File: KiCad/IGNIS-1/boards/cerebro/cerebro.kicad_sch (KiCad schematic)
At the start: 22 parts, among them J1 LiPo_1S_in, J2 RBF_pin, J40 Backplane_2x10, Q1 MMBT3904, SW1 Main_SW, U1 Prot_1S_UVLO_OCP, U10 ESP32-WROOM DevKit 38p, U2 BuckBoost_3V3, U3 Boost_5V

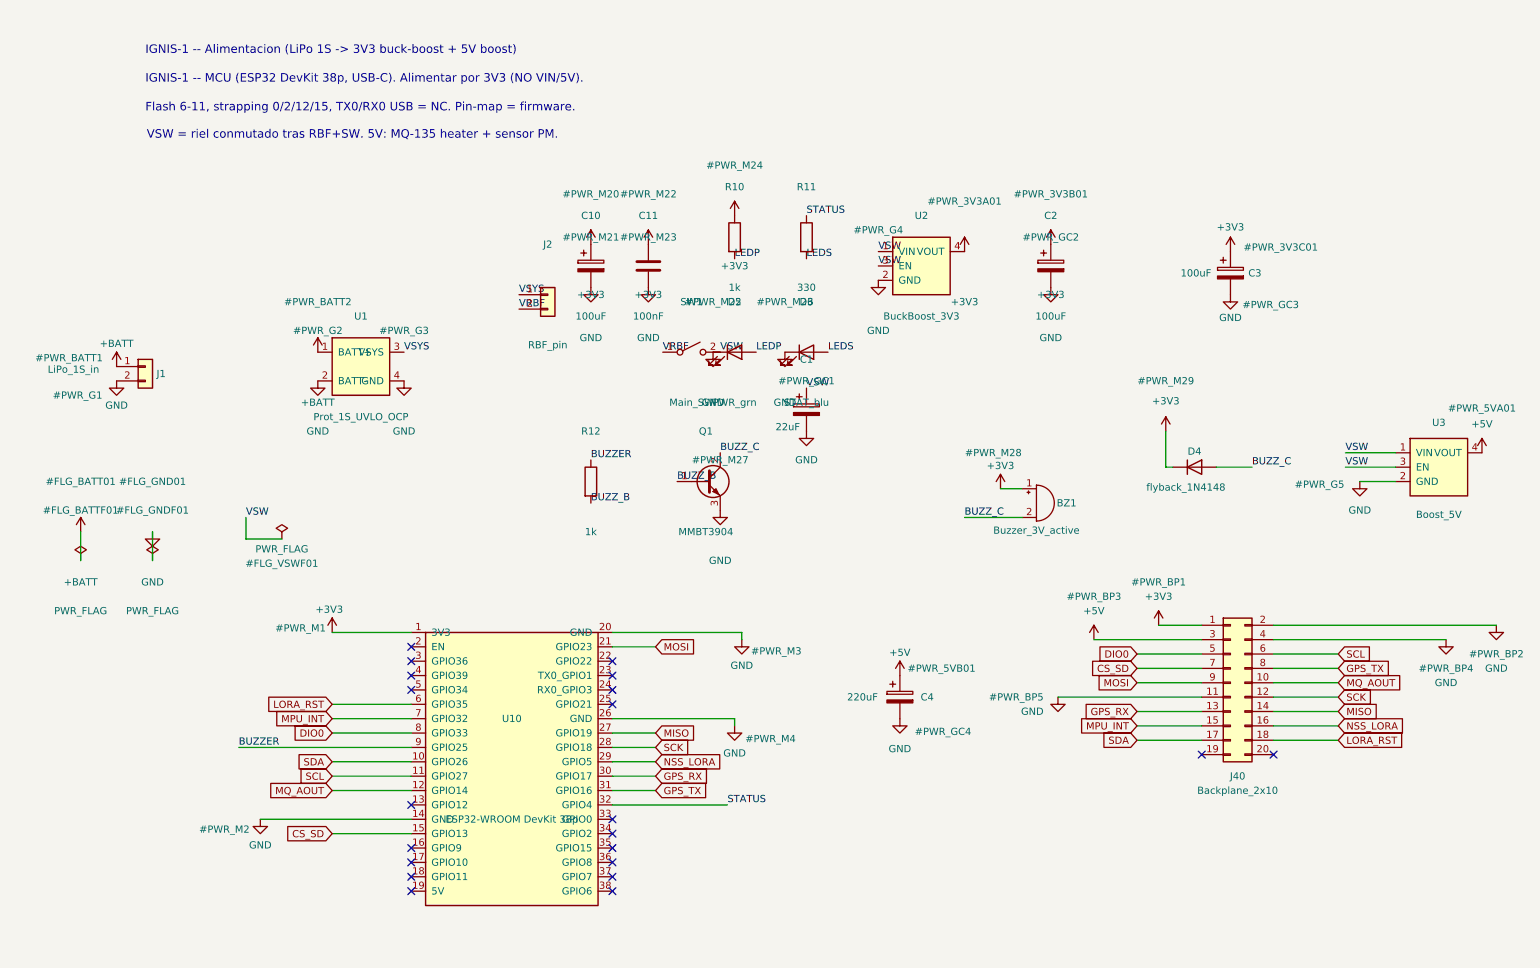
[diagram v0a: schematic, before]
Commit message: PCB del MCU creado
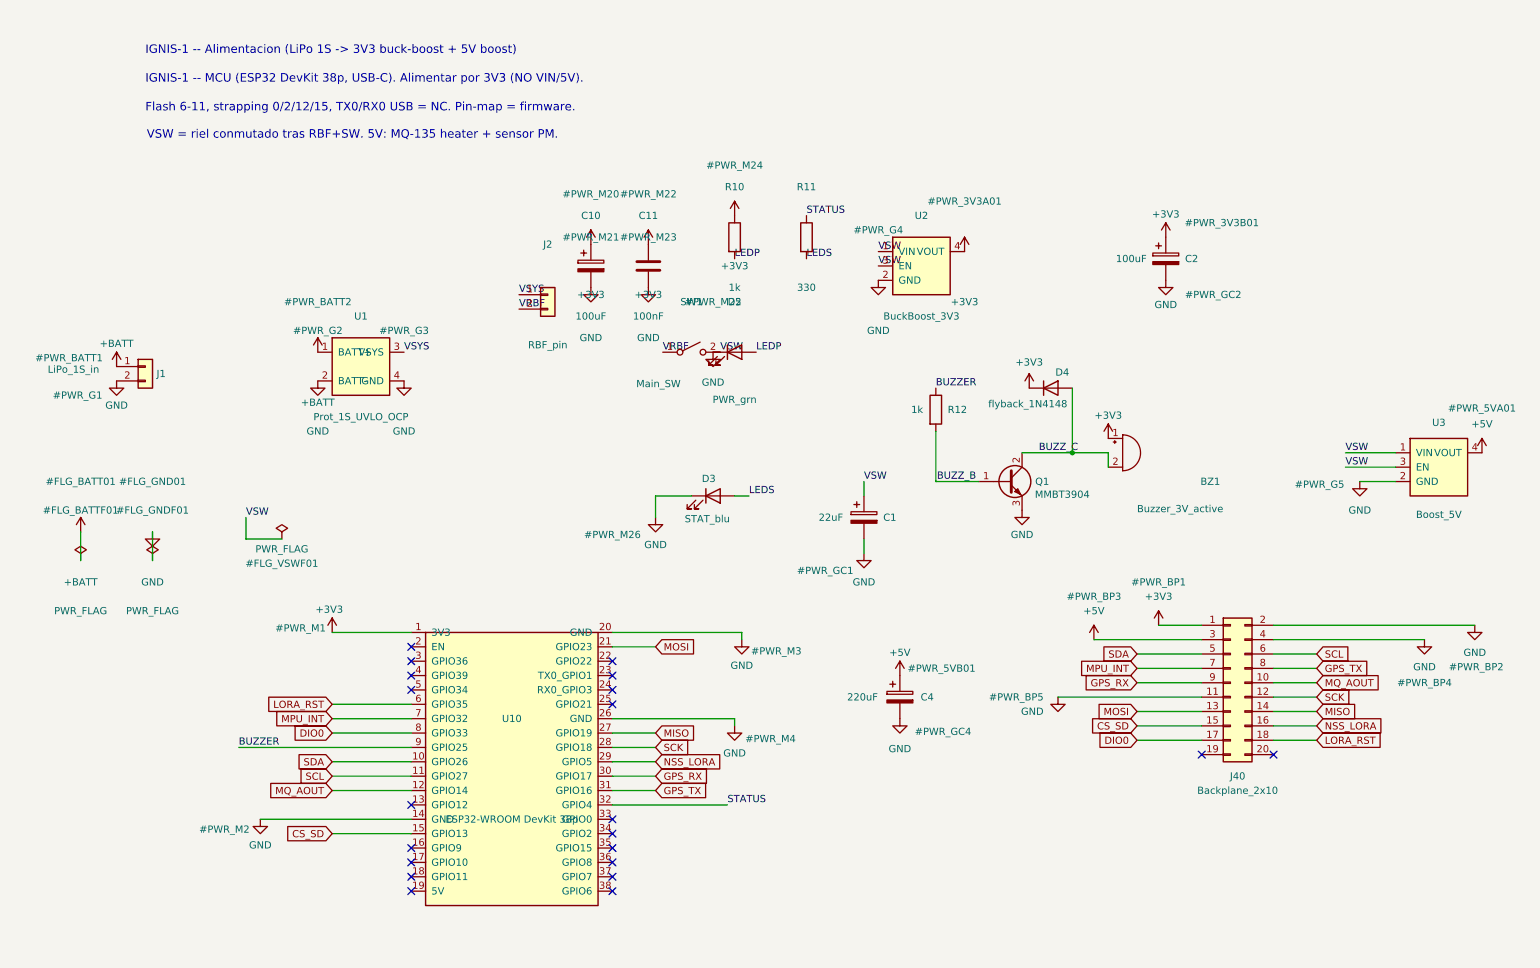
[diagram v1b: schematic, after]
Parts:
- removed C3: 100uF, Capacitor_THT:CP_Radial_D6.3mm_P2.50mm, symbol Device:C_Polarized
- U1, U2, U3: footprint (none) -> Connector_PinHeader_2.54mm:PinHeader_1x04_P2.54mm_Vertical
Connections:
- net CS_SD: now also J40.15 (Pin_15); no longer J40.7 (Pin_7)
- net DIO0: now also J40.17 (Pin_17); no longer J40.5 (Pin_5)
- net GPS_RX: now also J40.9 (Pin_9); no longer J40.13 (Pin_13)
- net MOSI: now also J40.13 (Pin_13); no longer J40.9 (Pin_9)
- net MPU_INT: now also J40.7 (Pin_7); no longer J40.15 (Pin_15)
- net SDA: now also J40.5 (Pin_5); no longer J40.17 (Pin_17)
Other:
- moved on the sheet: BZ1, C1, C2, D3, D4, Q1, R12

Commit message: Pines corregidos en ESP32
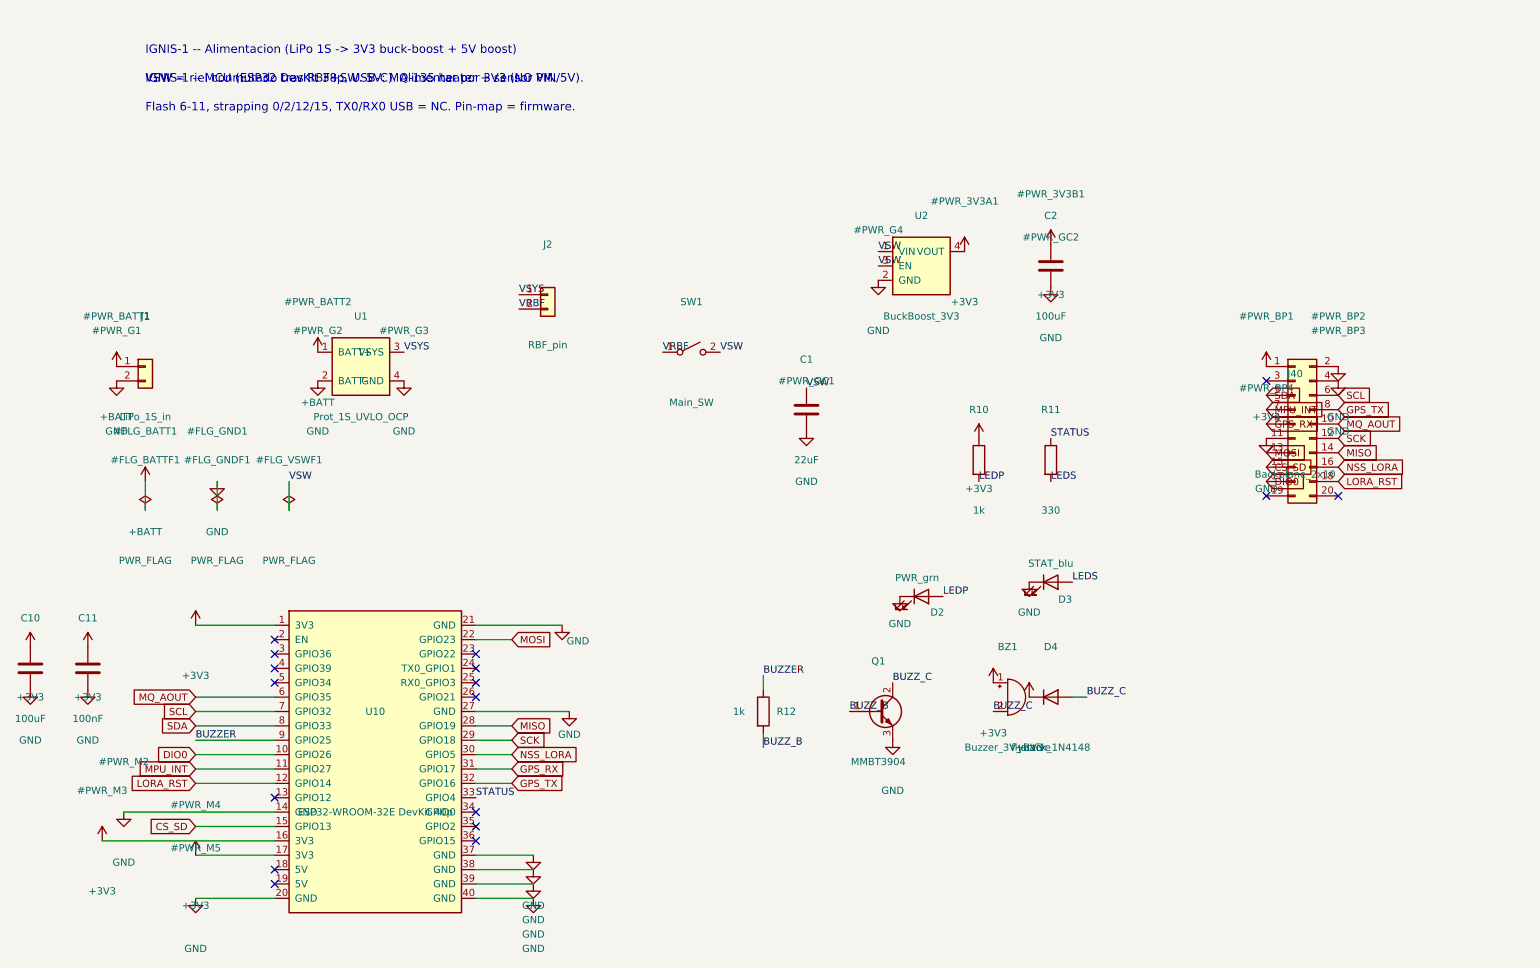
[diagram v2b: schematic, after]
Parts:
- removed C1: 22uF, Capacitor_THT:CP_Radial_D6.3mm_P2.50mm, symbol Device:C_Polarized
- removed C10, C2: 100uF, Capacitor_THT:CP_Radial_D6.3mm_P2.50mm, symbol Device:C_Polarized
- removed C4: 220uF, Capacitor_THT:CP_Radial_D6.3mm_P2.50mm, symbol Device:C_Polarized
- removed U10: ESP32-WROOM DevKit 38p, IGNIS1:ESP32_DevKit_38p, symbol IGNIS1:ESP32_DevKit_38
- removed U3: Boost_5V, Connector_PinHeader_2.54mm:PinHeader_1x04_P2.54mm_Vertical, symbol IGNIS1:DCDC_Module
- added C1: 22uF, Capacitor_SMD:C_0805_2012Metric, symbol Device:C
- added C10, C2: 100uF, Capacitor_SMD:C_1210_3225Metric, symbol Device:C
- added U10: ESP32-WROOM-32E DevKit 40p, IGNIS1:ESP32_DevKit_40p, symbol IGNIS1:ESP32_DevKit_40
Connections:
- net +3V3: now also C10.1, C2.1, U10.1 (3V3), U10.16 (3V3), U10.17 (3V3)
- net BUZZER: now also U10.9 (GPIO25)
- net CS_SD: now also U10.15 (GPIO13)
- net DIO0: now also U10.10 (GPIO26)
- net GND: now also C1.2, C10.2, C2.2, U10.14 (GND), U10.20 (GND), U10.21 (GND), U10.27 (GND), U10.37 (GND), U10.38 (GND), U10.39 (GND), U10.40 (GND)
- net GPS_RX: now also U10.31 (GPIO17)
- net GPS_TX: now also U10.32 (GPIO16)
- net LORA_RST: now also U10.12 (GPIO14)
- net MISO: now also U10.28 (GPIO19)
- net MOSI: now also U10.22 (GPIO23)
- net MPU_INT: now also U10.11 (GPIO27)
- net MQ_AOUT: now also U10.6 (GPIO35)
- net NSS_LORA: now also U10.30 (GPIO5)
- net SCK: now also U10.29 (GPIO18)
- net SCL: now also U10.7 (GPIO32)
- net SDA: now also U10.8 (GPIO33)
- net STATUS: now also U10.33 (GPIO4)
- net VSW: now also C1.1
- net +5V: no longer names the net of J40.3 (Pin_3)
- no-connect marks 21 -> 17

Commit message: Schematic arreglado. Footprint del ESP32 ajustado.
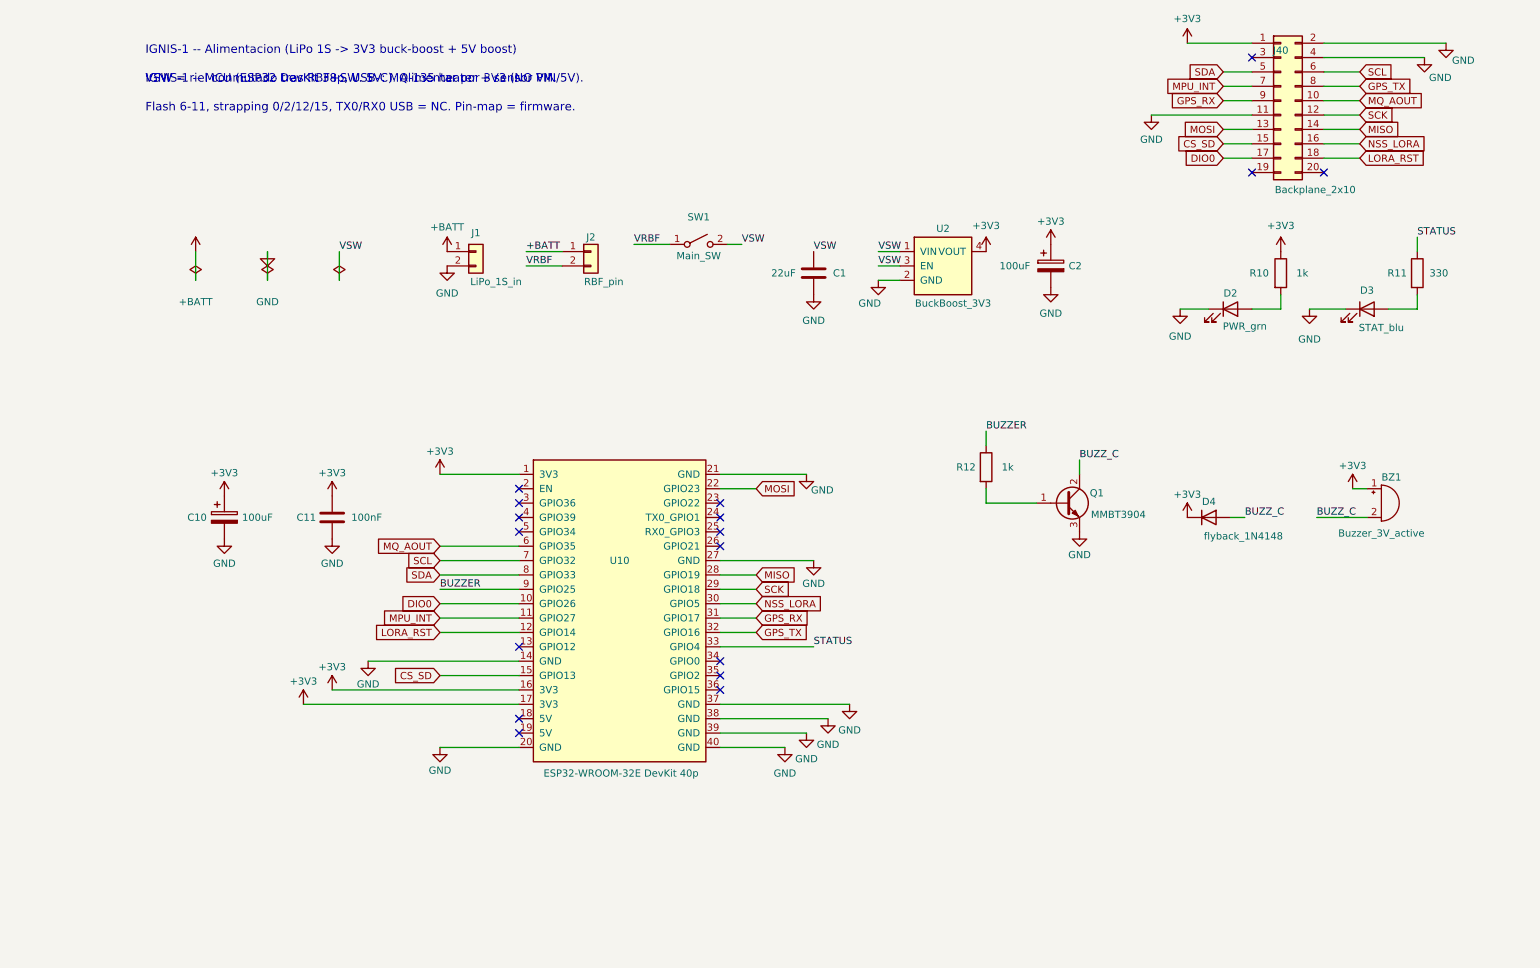
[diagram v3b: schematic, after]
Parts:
- removed U1: Prot_1S_UVLO_OCP, Connector_PinHeader_2.54mm:PinHeader_1x04_P2.54mm_Vertical, symbol IGNIS1:BattProtect_1S
- C1, C11: footprint Capacitor_SMD:C_0805_2012Metric -> Capacitor_SMD:C_0805_2012Metric_Pad1.18x1.45mm_HandSolder
- C10, C2: footprint Capacitor_SMD:C_1210_3225Metric -> Capacitor_THT:CP_Radial_D5.0mm_P2.00mm; symbol Device:C -> Device:C_Polarized
- D2, D3: footprint LED_SMD:LED_0805_2012Metric -> LED_SMD:LED_0805_2012Metric_Pad1.15x1.40mm_HandSolder
- R10, R11, R12: footprint Resistor_SMD:R_0805_2012Metric -> Resistor_SMD:R_0805_2012Metric_Pad1.20x1.40mm_HandSolder
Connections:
- net VSYS is gone; now on net +BATT: J2.1 (Pin_1)
- net BUZZ_B: no longer names the net of Q1.1 (B), R12.2
- net LEDP: no longer names the net of D2.2 (A), R10.2
- net LEDS: no longer names the net of D3.2 (A), R11.2
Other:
- moved on the sheet: BZ1, C1, C11, D2, D3, D4, J1, J2, J40, Q1, R10, R11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
